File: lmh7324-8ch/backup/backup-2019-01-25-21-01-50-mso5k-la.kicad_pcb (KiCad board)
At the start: 4 copper layers, 155 parts, among them IC201 lmh7324, IC301 lmh7324, IC401 lmh7324, IC501 lmh7324, J101 output, J102 input

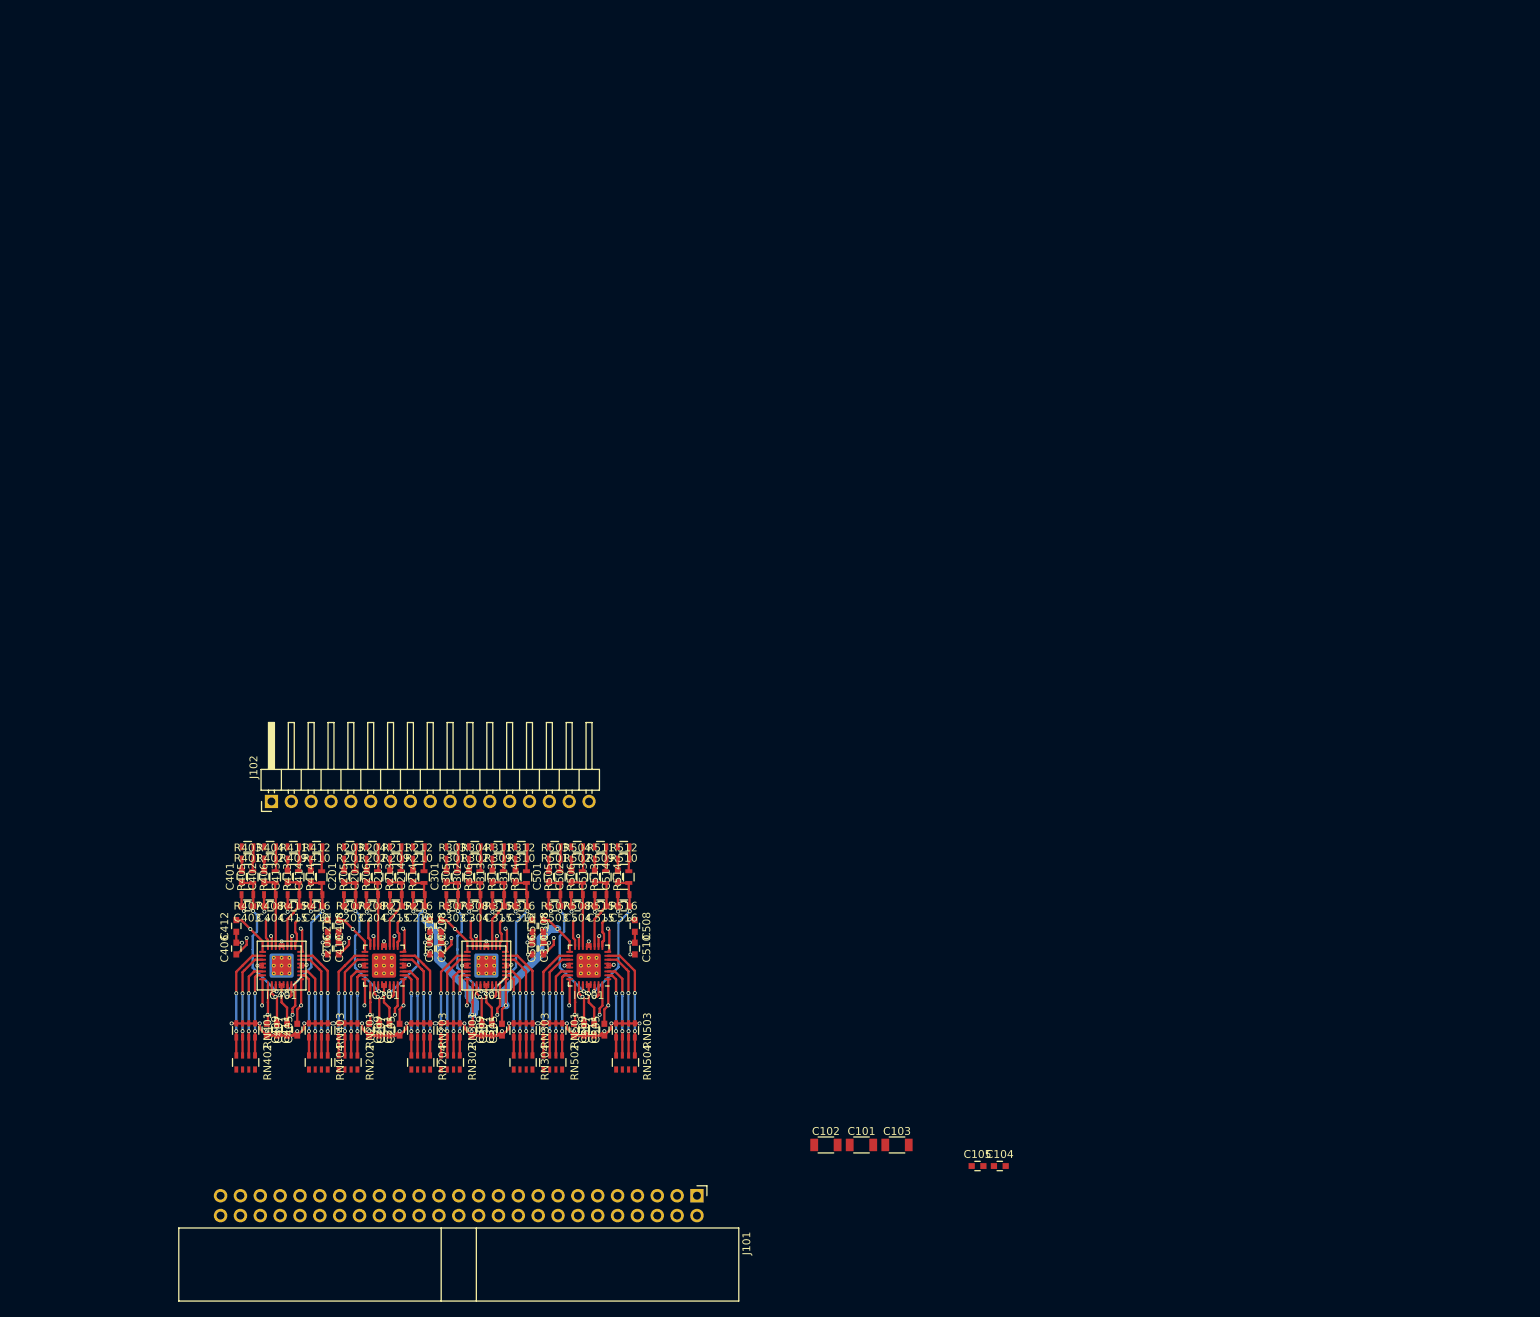
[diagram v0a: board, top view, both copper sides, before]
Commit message: Laid out the 8ch LMH7324 version and added a threshold display too
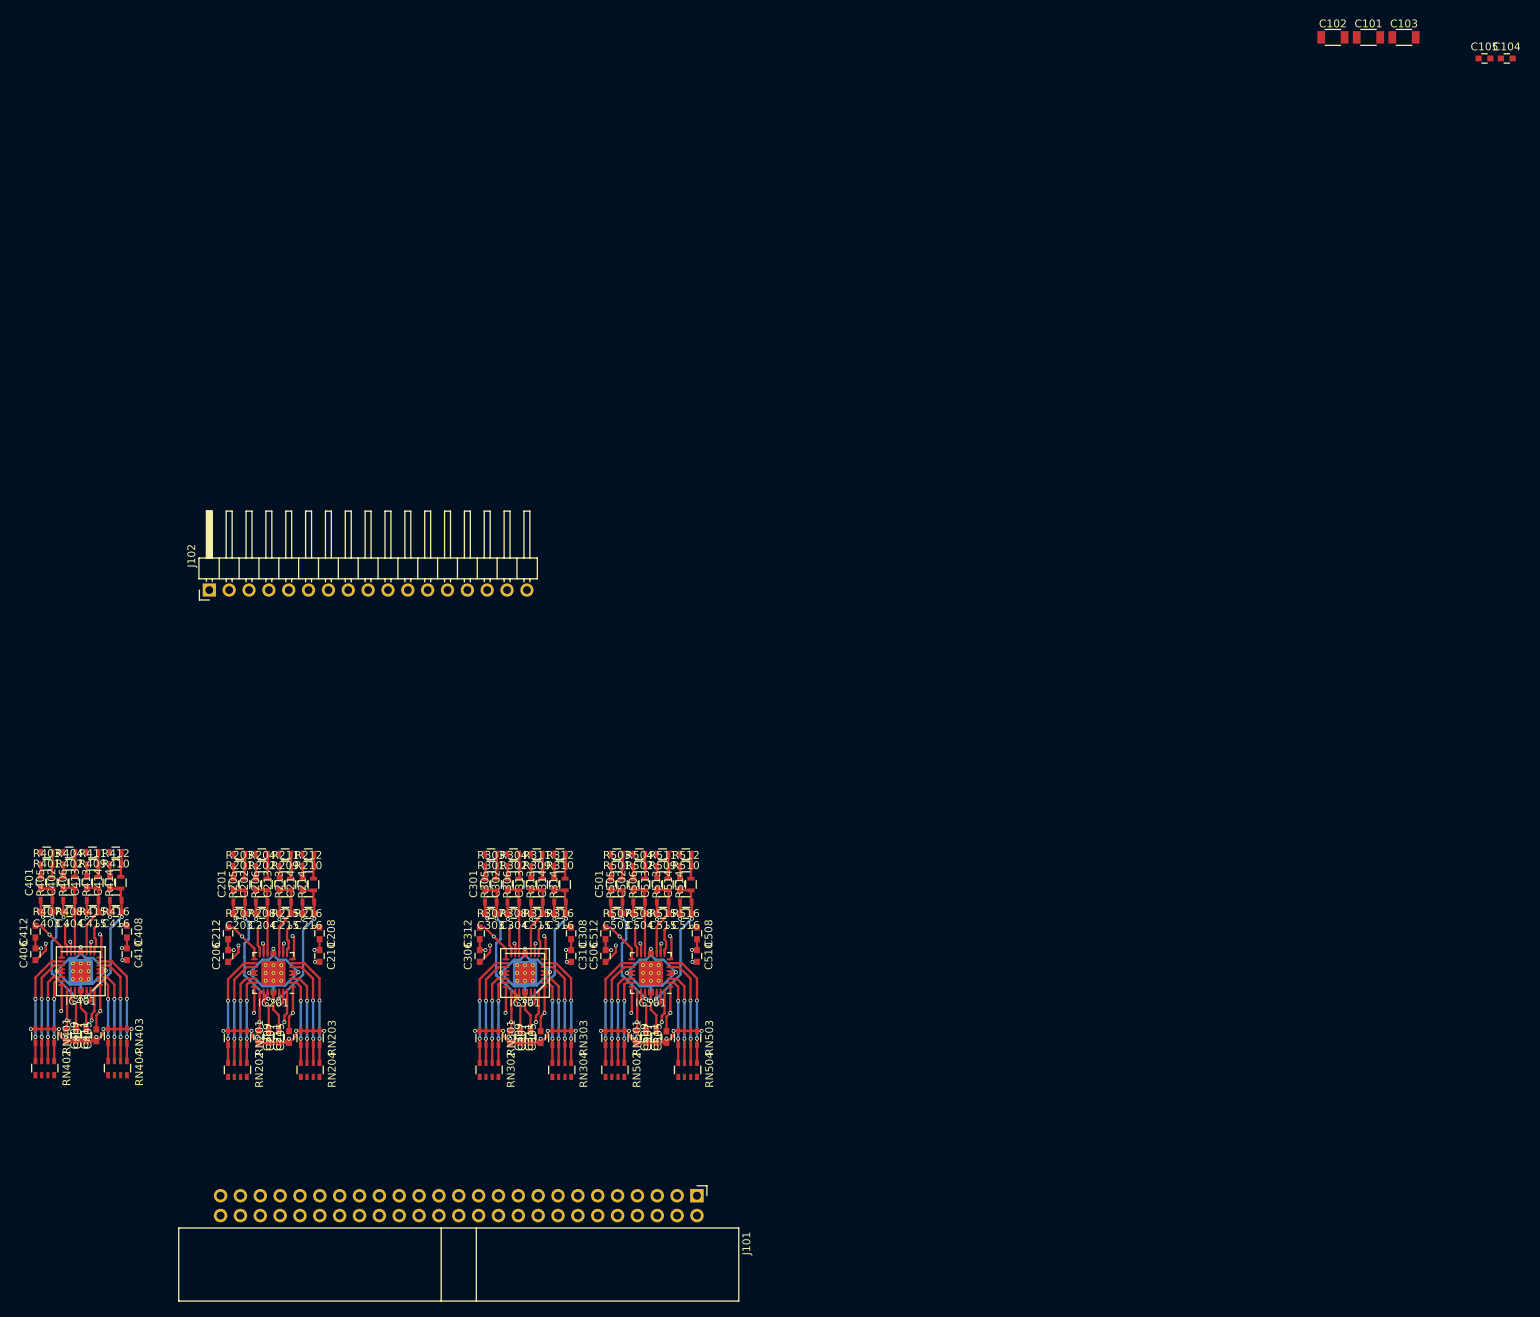
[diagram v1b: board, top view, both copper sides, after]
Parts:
- moved C101 155.9 mm to (197.5, 48.7)
- moved C102 155.9 mm to (193.0, 48.7)
- moved C103 155.9 mm to (202.1, 48.7)
- moved C104 155.9 mm to (215.2, 51.4)
- moved C105 155.9 mm to (212.4, 51.4)
- moved J102 28.2 mm to (49.2, 119.4)
- moved IC401 25.7 mm to (32.8, 168.2)
- moved R403 25.7 mm to (28.4, 154.6)
- moved R404 25.7 mm to (31.3, 154.6)
- moved R411 25.7 mm to (34.3, 154.6)
- moved C401 25.7 mm to (27.6, 156.8)
- moved C402 25.7 mm to (30.5, 156.8)
- moved C403 25.7 mm to (28.4, 160.6)
- moved C405 25.7 mm to (32.1, 176.4)
- moved C411 25.7 mm to (34.8, 176.4)
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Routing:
- net -2V5: track 142.0 -> 200.5 mm
- net +4V: track 189.7 -> 174.7 mm
- net +2V5: track 192.5 -> 179.2 mm
- net Vref_0-7: track 69.3 -> 80.7 mm
- net Vref_8-15: track 72.0 -> 80.7 mm
- removed copper zone on 3_Misc, net -2V5
